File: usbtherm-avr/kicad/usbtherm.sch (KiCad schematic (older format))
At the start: 18 parts, among them IC1 ATMEGA328-P, P1 USB_A, Q1 TMP36, Y1 12 MHz

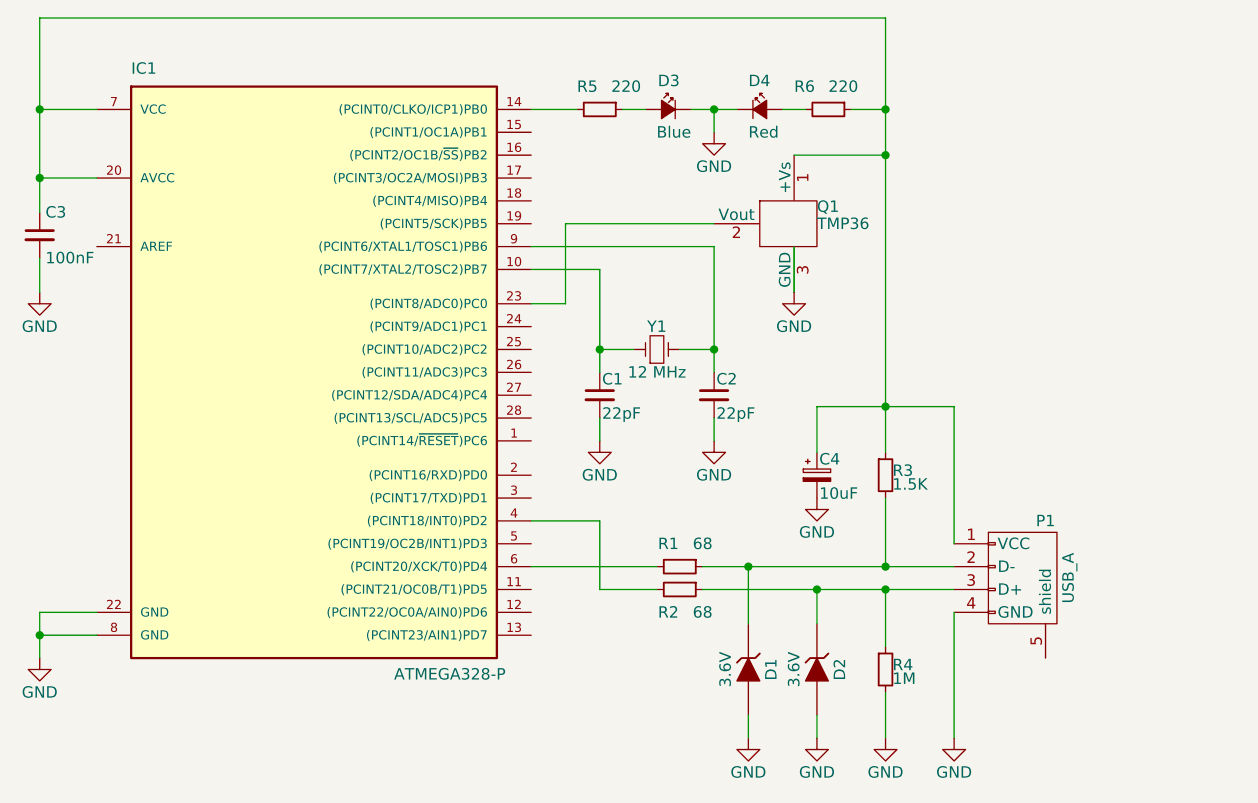
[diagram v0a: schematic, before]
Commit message: replaced USB connector with plug, created footprint for it, added board edges, autorouted with FreeRouting, fixed offset of 3D model of resistors
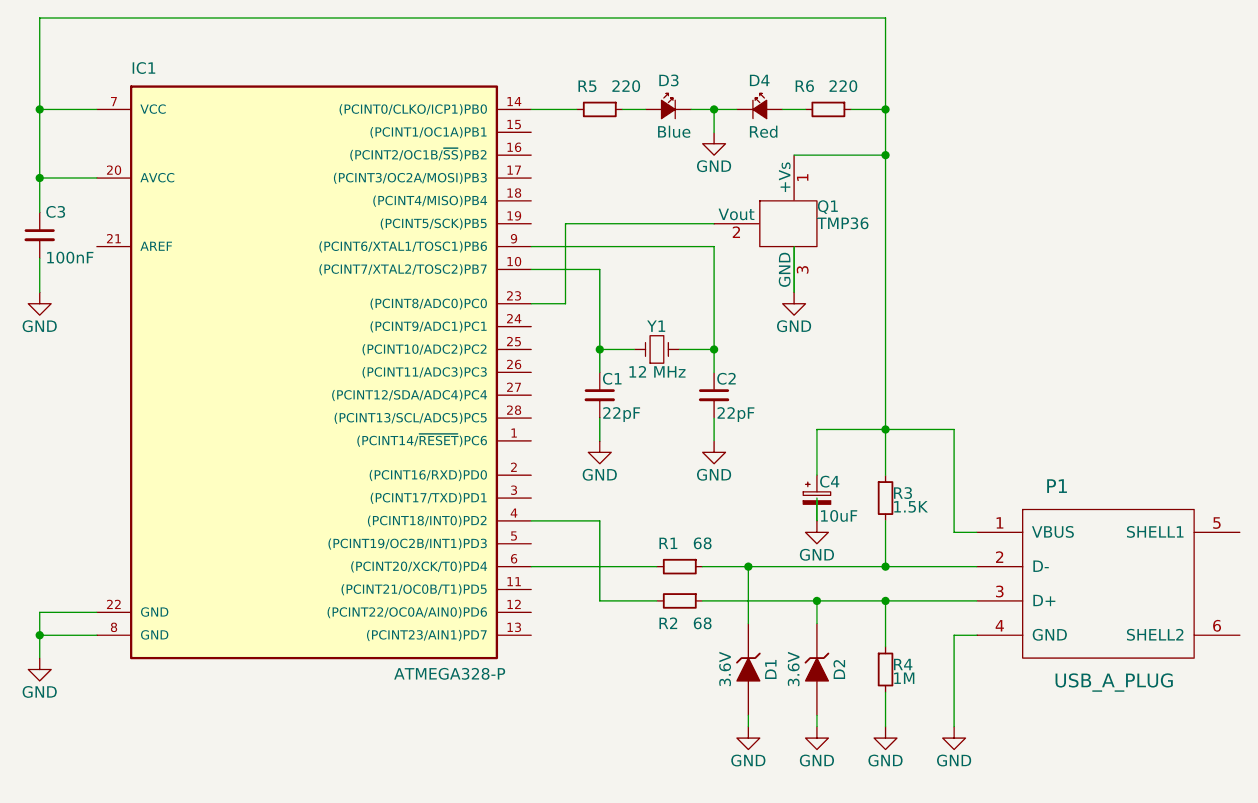
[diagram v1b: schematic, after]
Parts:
- removed P1: USB_A, Connect:USB_A, symbol USB_A
- added P1: USB_A_PLUG, Connect:USB_A_PLUG, symbol MOLEX_0480371000
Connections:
- wire segments 46 -> 48
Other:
- moved on the sheet: C4, R2, R3
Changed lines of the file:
@@
 LIBS:contrib
 LIBS:valves
+LIBS:usb_a_plug
+LIBS:usbtherm-cache
 EELAYER 25 0
 EELAYER END
@@
 Comment2 "Based on Metaboard https://metalab.at/wiki/Metaboard"
 Comment3 ""
-Comment4 ""
+Comment4 "Y1 can also be 16 MHz"
 $EndDescr
 $Comp
@@
 $EndComp
 $Comp
-L USB_A P1
-U 1 1 575C6667
-P 8500 5300
-F 0 "P1" V 8200 5400 50  0000 C CNN
-F 1 "USB_A" H 8450 5500 50  0000 C CNN
-F 2 "Connect:USB_A" V 8450 5200 50  0001 C CNN
-F 3 "" V 8450 5200 50  0000 C CNN
-	1    8500 5300
-	0    1    1    0
-$EndComp
-$Comp
 L GND #PWR01
 U 1 1 575C7B02
@@
 L R_Small R2
 U 1 1 575C85D0
-P 7000 5300
-F 0 "R2" V 7100 5250 50  0000 C CNN
-F 1 "68" V 7100 5400 50  0000 C CNN
-F 2 "Resistors_ThroughHole:Resistor_Horizontal_RM10mm" V 6930 5300 50  0001 C CNN
-F 3 "" H 7000 5300 50  0000 C CNN
-	1    7000 5300
+P 7000 5350
+F 0 "R2" V 7100 5300 50  0000 C CNN
+F 1 "68" V 7100 5450 50  0000 C CNN
+F 2 "Resistors_ThroughHole:Resistor_Horizontal_RM10mm" V 6930 5350 50  0001 C CNN
+F 3 "" H 7000 5350 50  0000 C CNN
+	1    7000 5350
 	0    1    1    0
 $EndComp
@@
 	6350 5000 6650 5000
 Wire Wire Line
-	6650 5000 6650 5300
+	6650 5000 6650 5350
 Wire Wire Line
 	6350 5200 6900 5200
 Wire Wire Line
-	7100 5200 8200 5200
-Wire Wire Line
-	6650 5300 6900 5300
-Wire Wire Line
-	7100 5300 8200 5300
+	7100 5200 8300 5200
+Wire Wire Line
+	6650 5350 6900 5350
+Wire Wire Line
+	7100 5350 8300 5350
 Wire Wire Line
 	4200 2800 4200 3650
@@
 	4200 2800 7900 2800
 Wire Wire Line
-	7900 2800 7900 4700
+	7900 2800 7900 4800
 Wire Wire Line
 	4200 3500 4450 3500
@@
 $EndComp
 Wire Wire Line
-	7600 5450 7600 5300
-Connection ~ 7600 5300
+	7600 5450 7600 5350
+Connection ~ 7600 5350
 $Comp
 L GND #PWR02
 U 1 1 575C8A05
-P 7600 5950
-F 0 "#PWR02" H 7600 5700 50  0001 C CNN
-F 1 "GND" H 7600 5800 50  0000 C CNN
-F 2 "" H 7600 5950 50  0000 C CNN
-F 3 "" H 7600 5950 50  0000 C CNN
-	1    7600 5950
+P 7600 5900
+F 0 "#PWR02" H 7600 5650 50  0001 C CNN
+F 1 "GND" H 7600 5750 50  0000 C CNN
+F 2 "" H 7600 5900 50  0000 C CNN
+F 3 "" H 7600 5900 50  0000 C CNN
+	1    7600 5900
 	1    0    0    -1
 $EndComp
@@
 L GND #PWR03
 U 1 1 575C8A2B
-P 7300 5950
-F 0 "#PWR03" H 7300 5700 50  0001 C CNN
-F 1 "GND" H 7300 5800 50  0000 C CNN
-F 2 "" H 7300 5950 50  0000 C CNN
-F 3 "" H 7300 5950 50  0000 C CNN
-	1    7300 5950
+P 7300 5900
+F 0 "#PWR03" H 7300 5650 50  0001 C CNN
+F 1 "GND" H 7300 5750 50  0000 C CNN
+F 2 "" H 7300 5900 50  0000 C CNN
+F 3 "" H 7300 5900 50  0000 C CNN
+	1    7300 5900
 	1    0    0    -1
 $EndComp
@@
 L GND #PWR04
 U 1 1 575C8A51
-P 8200 5950
-F 0 "#PWR04" H 8200 5700 50  0001 C CNN
-F 1 "GND" H 8200 5800 50  0000 C CNN
-F 2 "" H 8200 5950 50  0000 C CNN
-F 3 "" H 8200 5950 50  0000 C CNN
-	1    8200 5950
-	1    0    0    -1
-$EndComp
-Wire Wire Line
-	8200 5400 8200 5950
-Wire Wire Line
-	7600 5850 7600 5950
-Wire Wire Line
-	7300 5850 7300 5950
+P 8200 5900
+F 0 "#PWR04" H 8200 5650 50  0001 C CNN
+F 1 "GND" H 8200 5750 50  0000 C CNN
+F 2 "" H 8200 5900 50  0000 C CNN
+F 3 "" H 8200 5900 50  0000 C CNN
+	1    8200 5900
+	1    0    0    -1
+$EndComp
+Wire Wire Line
+	8200 5500 8200 5900
+Wire Wire Line
+	7600 5850 7600 5900
+Wire Wire Line
+	7300 5850 7300 5900
 $Comp
 L C_Small C3
@@
 L R_Small R3
 U 1 1 575C983C
-P 7900 4800
-F 0 "R3" H 7930 4820 50  0000 L CNN
-F 1 "1.5K" H 7930 4760 50  0000 L CNN
-F 2 "Resistors_ThroughHole:Resistor_Horizontal_RM10mm" H 7900 4800 50  0001 C CNN
-F 3 "" H 7900 4800 50  0000 C CNN
-	1    7900 4800
-	1    0    0    -1
-$EndComp
-Wire Wire Line
-	7600 4500 8200 4500
-Connection ~ 7900 4500
-Wire Wire Line
-	7900 4900 7900 5200
+P 7900 4900
+F 0 "R3" H 7930 4920 50  0000 L CNN
+F 1 "1.5K" H 7930 4860 50  0000 L CNN
+F 2 "Resistors_ThroughHole:Resistor_Horizontal_RM10mm" H 7900 4900 50  0001 C CNN
+F 3 "" H 7900 4900 50  0000 C CNN
+	1    7900 4900
+	1    0    0    -1
+$EndComp
+Wire Wire Line
+	7600 4600 8200 4600
+Connection ~ 7900 4600
+Wire Wire Line
+	7900 5000 7900 5200
 Connection ~ 7900 5200
 $Comp
@@
 $EndComp
 Wire Wire Line
-	7900 5550 7900 5300
-Connection ~ 7900 5300
+	7900 5550 7900 5350
+Connection ~ 7900 5350
 $Comp
 L GND #PWR08
 U 1 1 575C9DE7
-P 7900 5950
-F 0 "#PWR08" H 7900 5700 50  0001 C CNN
-F 1 "GND" H 7900 5800 50  0000 C CNN
-F 2 "" H 7900 5950 50  0000 C CNN
-F 3 "" H 7900 5950 50  0000 C CNN
-	1    7900 5950
-	1    0    0    -1
-$EndComp
-Wire Wire Line
-	7900 5750 7900 5950
-Wire Wire Line
-	8200 4500 8200 5100
+P 7900 5900
+F 0 "#PWR08" H 7900 5650 50  0001 C CNN
+F 1 "GND" H 7900 5750 50  0000 C CNN
+F 2 "" H 7900 5900 50  0000 C CNN
+F 3 "" H 7900 5900 50  0000 C CNN
+	1    7900 5900
+	1    0    0    -1
+$EndComp
+Wire Wire Line
+	7900 5750 7900 5900
+Wire Wire Line
+	8200 4600 8200 5050
 $Comp
 L CP_Small C4
 U 1 1 575CA3DE
-P 7600 4800
-F 0 "C4" H 7610 4870 50  0000 L CNN
-F 1 "10uF" H 7610 4720 50  0000 L CNN
-F 2 "Capacitors_ThroughHole:C_Radial_D5_L6_P2.5" H 7600 4800 50  0001 C CNN
-F 3 "" H 7600 4800 50  0000 C CNN
-	1    7600 4800
+P 7600 4900
+F 0 "C4" H 7610 4970 50  0000 L CNN
+F 1 "10uF" H 7610 4820 50  0000 L CNN
+F 2 "Capacitors_ThroughHole:C_Radial_D5_L6_P2.5" H 7600 4900 50  0001 C CNN
+F 3 "" H 7600 4900 50  0000 C CNN
+	1    7600 4900
 	1    0    0    -1
 $EndComp
@@
 L GND #PWR09
 U 1 1 575CA472
-P 7600 4900
-F 0 "#PWR09" H 7600 4650 50  0001 C CNN
-F 1 "GND" H 7600 4750 50  0000 C CNN
-F 2 "" H 7600 4900 50  0000 C CNN
-F 3 "" H 7600 4900 50  0000 C CNN
-	1    7600 4900
-	1    0    0    -1
-$EndComp
-Wire Wire Line
-	7600 4900 7600 4900
-Wire Wire Line
-	7600 4700 7600 4500
+P 7600 5000
+F 0 "#PWR09" H 7600 4750 50  0001 C CNN
+F 1 "GND" H 7600 4850 50  0000 C CNN
+F 2 "" H 7600 5000 50  0000 C CNN
+F 3 "" H 7600 5000 50  0000 C CNN
+	1    7600 5000
+	1    0    0    -1
+$EndComp
+Wire Wire Line
+	7600 5000 7600 4900
+Wire Wire Line
+	7600 4800 7600 4600
 $Comp
 L TMP36 Q1
@@
 Wire Wire Line
 	4450 3200 4200 3200
+$Comp
+L MOLEX_0480371000 P1
+U 1 1 575D87A1
+P 8900 5300
+F 0 "P1" H 8650 5750 60  0000 C CNN
+F 1 "USB_A_PLUG" H 8900 4900 60  0000 C CNN
+F 2 "Connect:USB_A_PLUG" H 8900 5300 60  0001 C CNN
+F 3 "" H 8900 5300 60  0000 C CNN
+	1    8900 5300
+	1    0    0    -1
+$EndComp
+Wire Wire Line
+	8200 5050 8300 5050
+Wire Wire Line
+	8300 5500 8200 5500
 $EndSCHEMATC
